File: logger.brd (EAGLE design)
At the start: 99 x 44.1 mm, 77 parts, among them IC1 LTC4412, J1 POWER_JACKPTH, Q1 FDN360P, Q2 FDN360P, Q3 2N7002PW, Q4 2N7002PW, U1 DS3231MZ/V+T, U2 FT231X-Q

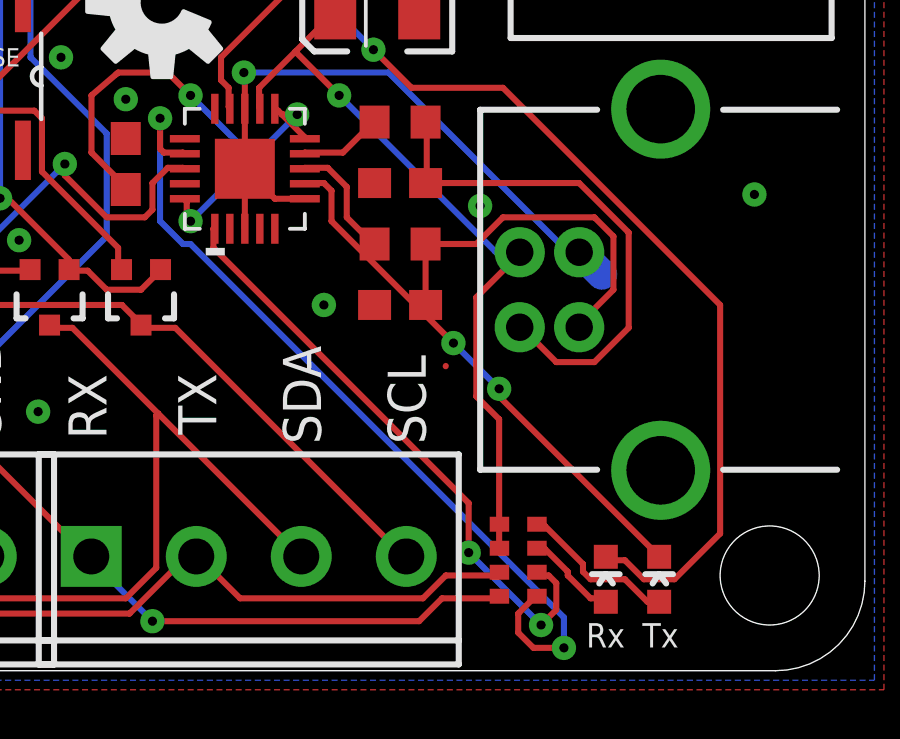
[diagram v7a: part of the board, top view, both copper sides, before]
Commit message: Fixed misrouted trace
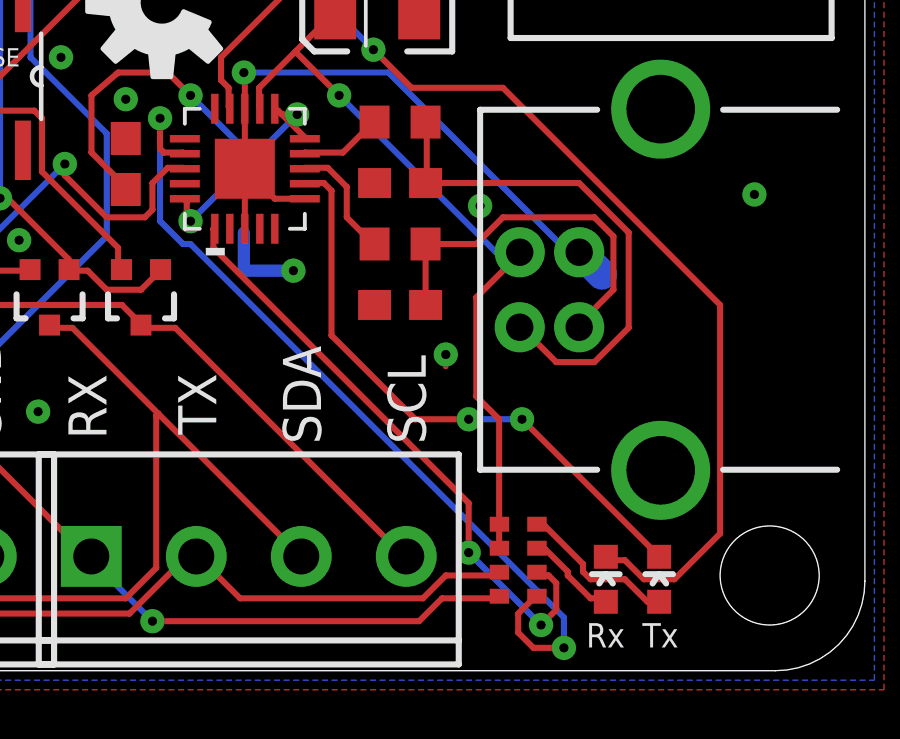
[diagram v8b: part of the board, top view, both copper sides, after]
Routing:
- net GND: track 57.6 -> 60.5 mm, vias 31 -> 32
- net N$6: track 17.7 -> 20.0 mm
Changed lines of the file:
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@@
 <wire x1="79.391" y1="15.732" x2="80.391" y2="15.732" width="0.2032" layer="1"/>
 <wire x1="78.391" y1="16.732" x2="78.391" y2="18.732" width="0.2032" layer="1"/>
-<via x="81.026" y="12.192" extent="1-16" drill="0.3048" shape="octagon"/>
+<via x="80.01" y="13.335" extent="1-16" drill="0.3048" shape="octagon"/>
+<via x="85.09" y="10.541" extent="1-16" drill="0.3048" shape="octagon"/>
+<wire x1="80.01" y1="13.335" x2="78.359" y2="13.335" width="0.4064" layer="16"/>
+<wire x1="78.359" y1="13.335" x2="78.359" y2="14.605" width="0.4064" layer="16"/>
 </signal>
 <signal name="5V">
@@
 <contactref element="LED2" pad="C"/>
 <contactref element="U2" pad="7"/>
-<wire x1="86.868" y1="9.144" x2="92.202" y2="3.81" width="0.2032" layer="1"/>
-<wire x1="86.868" y1="9.398" x2="86.868" y2="9.144" width="0.2032" layer="1"/>
-<wire x1="85.344" y1="10.922" x2="86.868" y2="9.398" width="0.2032" layer="16"/>
-<wire x1="81.28" y1="14.986" x2="85.344" y2="10.922" width="0.2032" layer="1"/>
-<wire x1="81.28" y1="16.002" x2="81.28" y2="14.986" width="0.2032" layer="1"/>
-<wire x1="81.026" y1="16.256" x2="81.28" y2="16.002" width="0.2032" layer="1"/>
-<wire x1="80.391" y1="16.256" x2="81.026" y2="16.256" width="0.2032" layer="1"/>
+<wire x1="87.63" y1="8.382" x2="92.202" y2="3.81" width="0.2032" layer="1"/>
+<wire x1="85.852" y1="8.382" x2="87.63" y2="8.382" width="0.2032" layer="16"/>
+<wire x1="83.947" y1="8.382" x2="84.074" y2="8.382" width="0.2032" layer="1"/>
+<wire x1="84.074" y1="8.382" x2="85.852" y2="8.382" width="0.2032" layer="1"/>
 <wire x1="92.202" y1="3.81" x2="92.202" y2="3.798" width="0.2032" layer="1"/>
+<via x="87.63" y="8.382" extent="1-16" drill="0.3048"/>
+<via x="85.852" y="8.382" extent="1-16" drill="0.3048"/>
+<wire x1="81.026" y1="16.256" x2="80.391" y2="16.256" width="0.2032" layer="1"/>
+<wire x1="81.28" y1="16.002" x2="81.026" y2="16.256" width="0.2032" layer="1"/>
+<wire x1="81.28" y1="11.176" x2="81.28" y2="16.002" width="0.2032" layer="1"/>
 <wire x1="80.391" y1="16.256" x2="80.391" y2="16.232" width="0.2032" layer="1"/>
-<via x="86.868" y="9.398" extent="1-16" drill="0.3048"/>
-<via x="85.344" y="10.922" extent="1-16" drill="0.3048"/>
+<wire x1="84.074" y1="8.382" x2="81.28" y2="11.176" width="0.2032" layer="1"/>
 </signal>
 <signal name="N$9">
